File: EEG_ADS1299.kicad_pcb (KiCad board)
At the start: 2 copper layers, 48.5 x 21.7 mm, 76 parts, among them IC1 ADS1299, P1 CONN_2, P2 CONN_2, P3 CONN_01X08, U1 TPS2294x, U2 TPS61222, U3 NRF528XX-QFAA, U4 MPU-9250, U5 INA828, U6 INA828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

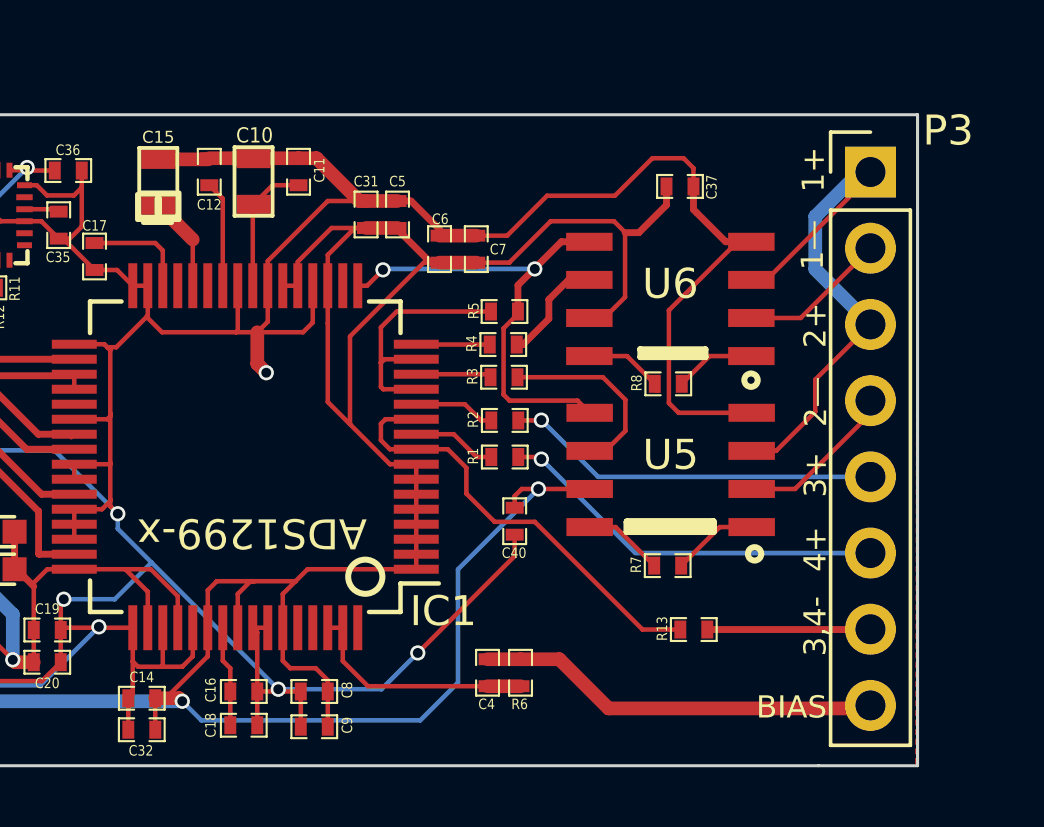
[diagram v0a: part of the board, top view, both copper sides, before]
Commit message: Removed extraneous components from sch and pcb.
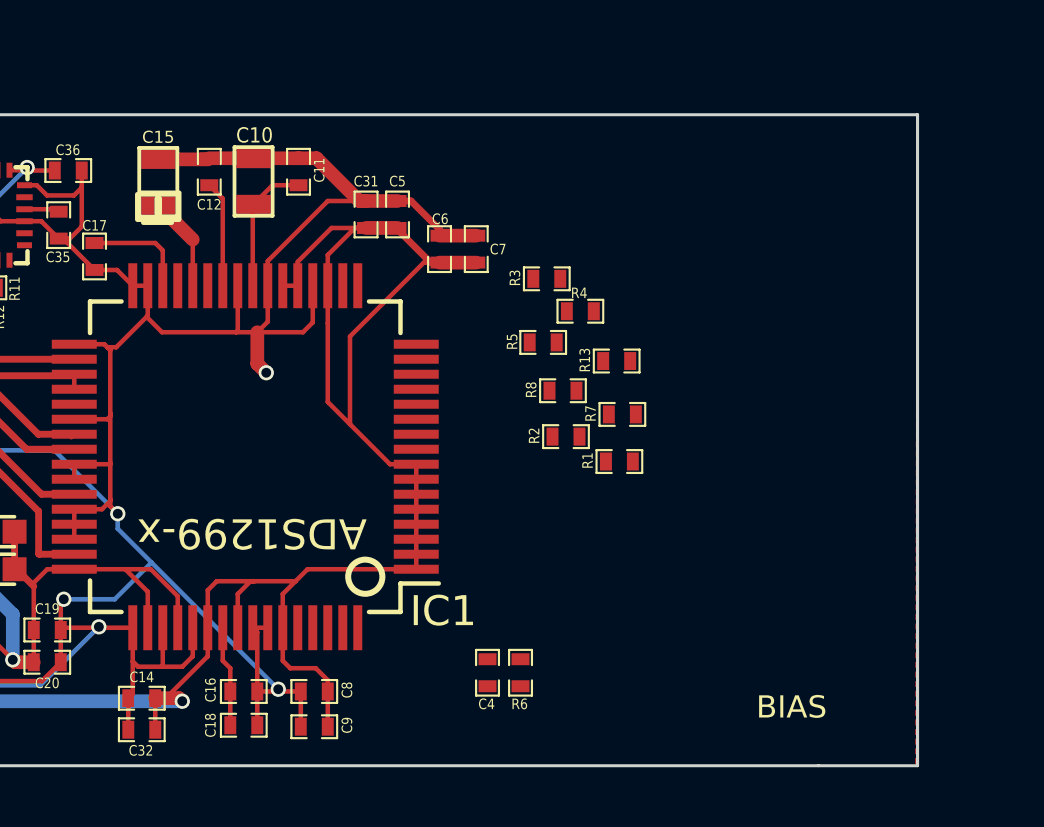
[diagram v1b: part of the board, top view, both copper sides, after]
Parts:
- removed C37, C40: 1uF, SM0402
- removed P3: CONN_01X08, Pin_Headers:Pin_Header_Straight_1x08_Pitch2.54mm
- removed U5, U6: INA828, INA828:SOIC_8_4.9mm_x_3.91
- R7, R8: value 10k -> 30k
- moved R13 9.31 mm to (304.4, 133.7)
- moved R7 5.26 mm to (304.6, 135.5)
- moved R1 3.82 mm to (304.5, 137.1)
- moved R3 3.58 mm to (302.1, 131.0)
- moved R8 3.52 mm to (302.6, 134.7)
- moved R4 2.80 mm to (303.2, 132.1)
- moved R2 2.11 mm to (302.7, 136.2)
- moved R5 1.65 mm to (301.9, 133.1)
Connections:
- net Net-(C4-Pad1) renamed /BIAS_ELEC
- C4 pad 2: /BIASIN -> Net-(C4-Pad2)
- IC1 pad 11: /IN3N -> Net-(IC1-Pad11)
- IC1 pad 13: /IN1N -> Net-(IC1-Pad13)
- IC1 pad 15: /IN1N -> Net-(IC1-Pad15)
- IC1 pad 17: /IN12- -> Net-(IC1-Pad17)
- IC1 pad 61: Net-(IC1-Pad61) -> Net-(C4-Pad2)
- IC1 pad 9: /IN3N -> Net-(IC1-Pad9)
- R1 pad 1: Net-(IC1-Pad10) -> Net-(IC1-Pad9)
- R1 pad 2: /IN4 -> Net-(R1-Pad2)
- R13 pad 1: /IN3N -> Net-(IC1-Pad13)
- R13 pad 2: /IN34- -> Net-(R13-Pad2)
- R2 pad 1: Net-(IC1-Pad12) -> Net-(IC1-Pad10)
- R2 pad 2: /IN3 -> Net-(R2-Pad2)
- R3 pad 1: Net-(IC1-Pad14) -> Net-(IC1-Pad16)
- R4 pad 1: Net-(IC1-Pad16) -> Net-(IC1-Pad15)
- R5 pad 1: /IN1N -> Net-(IC1-Pad14)
- R5 pad 2: /IN12- -> Net-(R5-Pad2)
- R6 pad 2: /BIASIN -> Net-(C4-Pad2)
- R7 pad 1: Net-(R7-Pad1) -> Net-(IC1-Pad11)
- R8 pad 1: Net-(R8-Pad1) -> Net-(IC1-Pad12)
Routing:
- net AVSS: track 230.4 -> 197.5 mm, vias 13 -> 12
- net AVDD: track 104.2 -> 72.0 mm, vias 3 -> 2
- net /REF_ELECTRODE: track 18.8 -> 0.00 mm
- net /IN12-: track 16.1 -> 0.00 mm, vias 2 -> 0
- net /IN3N: track 15.0 -> 0.00 mm
- net /BIASIN: track 13.5 -> 0.00 mm
- net /IN4: track 13.1 -> 0.00 mm, vias 1 -> 0
- net /IN3: track 12.5 -> 0.00 mm, vias 1 -> 0
- net /IN1N: track 8.31 -> 0.00 mm
- net /BIAS_ELEC: track 8.02 -> 0.14 mm
- net Net-(R3-Pad2): track 6.41 -> 0.00 mm
- net /IN34-: track 5.44 -> 0.00 mm
- net /IN2-: track 5.43 -> 0.00 mm
- net /IN1-: track 4.93 -> 0.00 mm
- net Net-(R4-Pad2): track 3.69 -> 0.00 mm
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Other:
- board text removed: "1+"
- board text removed: "1—"
- board text removed: "2+"
- board text removed: "2—"
- board text removed: "3+"
- board text removed: "3,4-"
- board text removed: "4+"

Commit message: Changed DFN-8 from 2x3mm to 3x2mm
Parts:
- added C37: 4.7uF, Capacitors_SMD:C_0402, F.Cu at (316.3, 116.3)
- added C40: 4.7uF, Capacitors_SMD:C_0402, F.Cu at (316.1, 118.6)
- added C41: 1.0uF, Capacitors_SMD:C_0402, F.Cu at (318.3, 116.3)
- added D3: D_Schottky, LEDs:LED_0603, F.Cu at (313.6, 118.7)
- added D4: LED, LEDs:LED_0603, F.Cu at (316.7, 115.0)
- added J1: Conn_01x08_Male, Pin_Headers:Pin_Header_Straight_2x04_Pitch2.54mm, F.Cu at (308.6, 130.4)
- added J2: Conn_01x02_Male, PIN_ARRAY_2X1, F.Cu at (318.4, 137.5)
- added P3: CONN_2, PIN_ARRAY_2X1, F.Cu at (319.0, 143.3)
- added Q1: DMP21D5UFB4-7B, pwrPad:X2-DFN1006, F.Cu at (317.6, 117.3)
- added R14: 2k, Resistors_SMD:R_0402, F.Cu at (316.1, 117.4)
- added R15: 100k, Resistors_SMD:R_0402, F.Cu at (319.0, 115.0)
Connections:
- IC1 pad 17: Net-(IC1-Pad17) -> /SRB1
- P1 pad 1: VCC -> /BATT_IN

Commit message: Added all components, and generated Gerbers.
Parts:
- added U5: MCP73831, Housings_DFN_QFN:DFN-8-1EP_3x2mm_Pitch0.5mm, F.Cu at (303.6, 142.0)
- C37, C40, C41: footprint Capacitors_SMD:C_0402 -> SM0402
- R14, R15: footprint Resistors_SMD:R_0402 -> SM0402
- moved P1 41.6 mm to (309.8, 143.6)
- moved R15 33.0 mm to (305.9, 145.3), turned to 180 degrees
- moved D4 32.9 mm to (301.3, 144.1), turned to 180 degrees
- moved C37 31.5 mm to (304.1, 145.3)
- moved R14 29.1 mm to (301.0, 142.3), turned to 90 degrees
- moved Q1 28.9 mm to (306.1, 143.8), turned to 180 degrees
- moved C41 27.7 mm to (307.7, 141.8), turned to 90 degrees
- moved D3 26.5 mm to (307.6, 144.5), turned to 270 degrees
- moved C40 25.2 mm to (306.4, 141.8), turned to 90 degrees
- moved J2 9.26 mm to (309.3, 138.9)
- moved P3 6.42 mm to (312.6, 143.6), turned to 90 degrees
- moved C4 6.07 mm to (303.8, 139.3), turned to 270 degrees
- moved R6 4.98 mm to (302.6, 139.3), turned to 270 degrees
- moved R4 3.28 mm to (305.3, 129.6)
- moved R3 3.00 mm to (303.7, 128.5)
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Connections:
- R1 pad 2: Net-(J1-Pad1) -> Net-(J1-Pad8)
- R13 pad 2: Net-(J1-Pad5) -> Net-(J1-Pad4)
- R2 pad 2: Net-(J1-Pad2) -> Net-(J1-Pad7)
- R3 pad 2: Net-(J1-Pad8) -> Net-(J1-Pad1)
- R4 pad 2: Net-(J1-Pad7) -> Net-(J1-Pad2)
- R5 pad 2: Net-(J1-Pad6) -> Net-(J1-Pad3)
- R7 pad 2: Net-(J1-Pad3) -> Net-(J1-Pad6)
- R8 pad 2: Net-(J1-Pad4) -> Net-(J1-Pad5)
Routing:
- net AVSS: track 197.5 -> 224.9 mm, vias 12 -> 13
- net DVDD: track 66.6 -> 93.0 mm, vias 7 -> 8
- net VCC: track 24.8 -> 50.4 mm, vias 0 -> 2
- net /BIAS_ELEC: track 0.14 -> 19.0 mm
- net /SRB1: track 0.00 -> 15.8 mm, vias 0 -> 1
- net 5V_in_charge: track 0.00 -> 14.9 mm
- net Net-(C4-Pad2): track 0.00 -> 12.2 mm
- net /BATT_IN: track 0.00 -> 9.26 mm, vias 0 -> 1
- net Net-(IC1-Pad15): track 0.00 -> 8.87 mm
- net Net-(IC1-Pad13): track 0.00 -> 8.49 mm
- net Net-(IC1-Pad11): track 0.07 -> 7.89 mm
- net Net-(IC1-Pad9): track 0.00 -> 7.66 mm
- net Net-(IC1-Pad16): track 0.00 -> 7.50 mm
- net Net-(IC1-Pad14): track 0.00 -> 6.93 mm
- net Net-(IC1-Pad12): track 0.00 -> 6.29 mm
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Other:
- outline, holes or cut-outs redrawn
- board text added: "+"
- board text added: "-"
- board text added: "1"
- board text added: "2"
- board text added: "3"
- board text added: "4"
- board text added: "5V+"
- board text added: "Bat+"
- board text added: "SRB1"
- board text added: "nRF52-ADS1299 with MPU ExG Prototype v4.0 Yeo BNE Lab - GaTech"
- board text removed: "VIN"
- board text removed: "nRF52-ADS1299-4 with MPU ExG Prototype v3.0 Yeo GaTech BNE Lab"

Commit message: Minor edits to finalize.
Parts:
- moved P2 21.2 mm to (300.5, 126.9)
- moved R3 0.40 mm to (303.5, 128.8)
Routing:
- net /SWDCLK: track 5.14 -> 26.1 mm, vias 0 -> 1
- net /SWDIO: track 5.20 -> 23.5 mm, vias 0 -> 1
- net AVSS: track 224.9 -> 221.3 mm, vias 13 -> 12
- net DVDD: track 93.0 -> 90.8 mm
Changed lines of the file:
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@@
     (thickness 1.6)
     (drawings 32)
-    (tracks 759)
+    (tracks 766)
     (zones 0)
     (modules 83)
@@
   )
   (setup
-    (last_trace_width 0.4572)
+    (last_trace_width 0.152)
     (user_trace_width 0.152)
     (user_trace_width 0.229)
@@
   )
   (module PIN_ARRAY_2X1 (layer F.Cu)
-    (at 279.3 126.45 180)
+    (at 300.51 126.93 180)
     (descr "Connecteurs 2 pins")
     (tags "CONN DEV")
@@
   )
   (module SM0402 (layer F.Cu)
-    (at 303.70958 128.47)
+    (at 303.53958 128.83)
     (attr smd)
     (fp_text reference R3 (at -1.05 -0.03 90) (layer F.SilkS)
@@
     )
   )
-  (gr_text I/O (at 275.72 126.25) (layer F.SilkS)
+  (gr_text I/O (at 297.28 126.56 90) (layer F.SilkS)
     (effects (font (size 0.7 0.7) (thickness 0.1)))
   )
@@
     (effects (font (size 1.5 1.5) (thickness 0.3)))
   )
-  (gr_text CLK (at 282.95 126.4) (layer F.SilkS)
+  (gr_text CLK (at 303.59 126.97 90) (layer F.SilkS)
     (effects (font (size 0.7 0.7) (thickness 0.1)))
   )
@@
   (segment (start 286.2 136.25) (end 286.3 136.15) (width 0.152) (layer F.Cu) (net 5))
   (segment (start 280 131) (end 280 130.73) (width 0.152) (layer F.Cu) (net 6))
-  (segment (start 280.57 126.51) (end 280.57 126.45) (width 0.152) (layer F.Cu) (net 6))
-  (segment (start 279.896811 127.183189) (end 280.57 126.51) (width 0.152) (layer F.Cu) (net 6))
-  (segment (start 279.896811 130.186811) (end 279.896811 127.183189) (width 0.152) (layer F.Cu) (net 6))
-  (segment (start 280 130.29) (end 279.896811 130.186811) (width 0.152) (layer F.Cu) (net 6))
-  (segment (start 280 131) (end 280 130.29) (width 0.152) (layer F.Cu) (net 6))
-  (segment (start 278.791999 127.211999) (end 278.03 126.45) (width 0.152) (layer F.Cu) (net 7))
-  (segment (start 279.592401 128.012401) (end 278.791999 127.211999) (width 0.152) (layer F.Cu) (net 7))
-  (segment (start 279.592401 130.622401) (end 279.592401 128.012401) (width 0.152) (layer F.Cu) (net 7))
-  (segment (start 279.6 130.63) (end 279.592401 130.622401) (width 0.152) (layer F.Cu) (net 7))
-  (segment (start 279.6 131) (end 279.6 130.63) (width 0.152) (layer F.Cu) (net 7))
+  (via (at 280.61 128.6) (size 0.508) (drill 0.3302) (layers F.Cu B.Cu) (net 6))
+  (segment (start 280 131) (end 280 129.21) (width 0.152) (layer F.Cu) (net 6))
+  (segment (start 280 129.21) (end 280.61 128.6) (width 0.152) (layer F.Cu) (net 6))
+  (segment (start 280.863999 128.346001) (end 282.503999 128.346001) (width 0.152) (layer B.Cu) (net 6))
+  (segment (start 280.61 128.6) (end 280.863999 128.346001) (width 0.152) (layer B.Cu) (net 6))
+  (segment (start 284.072401 126.777599) (end 296.697599 126.777599) (width 0.152) (layer B.Cu) (net 6))
+  (segment (start 282.503999 128.346001) (end 284.072401 126.777599) (width 0.152) (layer B.Cu) (net 6))
+  (segment (start 296.697599 126.777599) (end 298.32 128.4) (width 0.152) (layer B.Cu) (net 6))
+  (segment (start 300.866 126.93) (end 301.78 126.93) (width 0.152) (layer B.Cu) (net 6))
+  (segment (start 299.396 128.4) (end 300.866 126.93) (width 0.152) (layer B.Cu) (net 6))
+  (segment (start 298.32 128.4) (end 299.396 128.4) (width 0.152) (layer B.Cu) (net 6))
+  (segment (start 279.6 131) (end 279.6 128.75) (width 0.152) (layer F.Cu) (net 7))
+  (via (at 280.64 127.33) (size 0.508) (drill 0.3302) (layers F.Cu B.Cu) (net 7))
+  (segment (start 279.6 128.75) (end 280.64 127.71) (width 0.152) (layer F.Cu) (net 7))
+  (segment (start 280.64 127.71) (end 280.64 127.33) (width 0.152) (layer F.Cu) (net 7))
+  (segment (start 280.893999 127.076001) (end 282.703999 127.076001) (width 0.152) (layer B.Cu) (net 7))
+  (segment (start 280.64 127.33) (end 280.893999 127.076001) (width 0.152) (layer B.Cu) (net 7))
+  (segment (start 298.478001 126.168001) (end 299.24 126.93) (width 0.152) (layer B.Cu) (net 7))
+  (segment (start 283.611999 126.168001) (end 298.478001 126.168001) (width 0.152) (layer B.Cu) (net 7))
+  (segment (start 282.703999 127.076001) (end 283.611999 126.168001) (width 0.152) (layer B.Cu) (net 7))
   (segment (start 280.8 135.8) (end 282.19 135.8) (width 0.229) (layer F.Cu) (net 8))
   (segment (start 285.13 140.15) (end 286.3 140.15) (width 0.229) (layer F.Cu) (net 8))
@@
   (via (at 282.12 136.98) (size 0.508) (drill 0.3302) (layers F.Cu B.Cu) (net 12))
   (segment (start 282.552 137.412) (end 282.12 136.98) (width 0.152) (layer F.Cu) (net 12))
-  (segment (start 279.11 128.53) (end 282.31 128.53) (width 0.152) (layer B.Cu) (net 12))
-  (segment (start 279.08 128.5) (end 279.11 128.53) (width 0.229) (layer F.Cu) (net 12))
-  (via (at 279.11 128.53) (size 0.508) (drill 0.3302) (layers F.Cu B.Cu) (net 12))
-  (segment (start 278.3265 128.5) (end 279.08 128.5) (width 0.229) (layer F.Cu) (net 12))
-  (via (at 282.57 128.27) (size 0.508) (drill 0.3302) (layers F.Cu B.Cu) (net 12))
-  (segment (start 282.31 128.53) (end 282.57 128.27) (width 0.152) (layer B.Cu) (net 12))
   (segment (start 282.57 128.27) (end 282.585 128.255) (width 0.152) (layer F.Cu) (net 12))
   (segment (start 282.585 128.255) (end 282.57 128.27) (width 0.152) (layer F.Cu) (net 12))
@@
   (segment (start 310.82763 142.37) (end 312.55 142.37) (width 0.152) (layer F.Cu) (net 12))
   (segment (start 309.75 142.37) (end 310.82763 142.37) (width 0.152) (layer F.Cu) (net 12))
+  (via (at 279.03 128.51) (size 0.508) (drill 0.3302) (layers F.Cu B.Cu) (net 12))
+  (segment (start 278.3265 128.5) (end 279.02 128.5) (width 0.152) (layer F.Cu) (net 12))
+  (segment (start 279.02 128.5) (end 279.03 128.51) (width 0.152) (layer F.Cu) (net 12))
   (segment (start 280.25 138.13) (end 280.25 138.15) (width 0.4572) (layer B.Cu) (net 13))
   (segment (start 284.25 142.15) (end 284.25 143.67) (width 0.4572) (layer B.Cu) (net 13))
@@
   (segment (start 288 140.65) (end 288.75 141.4) (width 0.152) (layer F.Cu) (net 13))
   (via (at 283.22 133.06) (size 0.508) (drill 0.3302) (layers F.Cu B.Cu) (net 13))
-  (segment (start 274.64 137.01) (end 279.27 137.01) (width 0.4572) (layer B.Cu) (net 13))
   (segment (start 279.27 137.01) (end 283.22 133.06) (width 0.4572) (layer B.Cu) (net 13))
   (segment (start 275.12 130.98) (end 275.12 136.45) (width 0.4572) (layer B.Cu) (net 13))
@@
   (segment (start 274.04958 129.45) (end 274.58 129.45) (width 0.152) (layer F.Cu) (net 13))
   (segment (start 275.14 131) (end 275.6 131) (width 0.152) (layer F.Cu) (net 13))
-  (via (at 299.69 144.07) (size 0.508) (drill 0.3302) (layers F.Cu B.Cu) (net 13))
-  (segment (start 300.53 144.08) (end 299.7 144.08) (width 0.152) (layer F.Cu) (net 13))
-  (segment (start 299.7 144.08) (end 299.69 144.07) (width 0.152) (layer F.Cu) (net 13))
-  (segment (start 299.69 144.07) (end 295.73 140.11) (width 0.152) (layer B.Cu) (net 13))
-  (segment (start 295.73 140.11) (end 295.73 134.05) (width 0.152) (layer B.Cu) (net 13))
-  (segment (start 288.94 127.26) (end 284.73 127.26) (width 0.152) (layer B.Cu) (net 13))
-  (segment (start 295.73 134.05) (end 288.94 127.26) (width 0.152) (layer B.Cu) (net 13))
+  (segment (start 274.64 137.01) (end 279.27 137.01) (width 0.4572) (layer B.Cu) (net 13))
+  (via (at 299.11 144.07) (size 0.508) (drill 0.3302) (layers F.Cu B.Cu) (net 13))
+  (segment (start 284.73 127.26) (end 284.73 129.69) (width 0.152) (layer B.Cu) (net 13))
+  (segment (start 284.73 129.69) (end 299.11 144.07) (width 0.152) (layer B.Cu) (net 13))
+  (segment (start 300.52 144.07) (end 300.53 144.08) (width 0.152) (layer F.Cu) (net 13))
+  (segment (start 299.11 144.07) (end 300.52 144.07) (width 0.152) (layer F.Cu) (net 13))
   (segment (start 298.475 130.42958) (end 297.95042 130.42958) (width 0.152) (layer F.Cu) (net 14))
   (segment (start 295.49 132.89) (end 295.49 135.815) (width 0.152) (layer F.Cu) (net 14))
@@
   (segment (start 300.10117 134.15) (end 303.23084 131.02033) (width 0.152) (layer F.Cu) (net 16))
   (segment (start 297.7 134.15) (end 300.10117 134.15) (width 0.152) (layer F.Cu) (net 16))
-  (segment (start 302.98 128.47) (end 303.26 128.47) (width 0.152) (layer F.Cu) (net 17))
-  (segment (start 298.3 133.15) (end 302.98 128.47) (width 0.152) (layer F.Cu) (net 17))
+  (segment (start 302.73861 128.83) (end 303.09 128.83) (width 0.152) (layer F.Cu) (net 17))
+  (segment (start 302.62 128.83) (end 302.73861 128.83) (width 0.152) (layer F.Cu) (net 17))
+  (segment (start 298.3 133.15) (end 302.62 128.83) (width 0.152) (layer F.Cu) (net 17))
   (segment (start 297.7 133.15) (end 298.3 133.15) (width 0.152) (layer F.Cu) (net 17))
   (segment (start 286.3 133.65) (end 281.71 133.65) (width 0.229) (layer F.Cu) (net 21))
@@
   (segment (start 296.75 130.77) (end 304.88 138.9) (width 0.152) (layer B.Cu) (net 100))
   (segment (start 307.97 128.47) (end 308.04 128.54) (width 0.152) (layer F.Cu) (net 101))
-  (segment (start 304.15916 128.47) (end 307.97 128.47) (width 0.152) (layer F.Cu) (net 101))
+  (segment (start 307.75 128.83) (end 308.04 128.54) (width 0.152) (layer F.Cu) (net 101))
+  (segment (start 303.98916 128.83) (end 307.75 128.83) (width 0.152) (layer F.Cu) (net 101))
   (segment (start 306.14055 129.59) (end 306.52055 129.97) (width 0.152) (layer F.Cu) (net 102))
   (segment (start 305.78916 129.59) (end 306.14055 129.59) (width 0.152) (layer F.Cu) (net 102))
